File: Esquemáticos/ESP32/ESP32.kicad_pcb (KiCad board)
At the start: 2 copper layers, 100 x 100 mm, 71 parts, among them J1 Conector para bobinas del mot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, J2 Conector para bobinas del mot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, J3 Barrel_Jack, J4 USB Programador, Q1 S8550, Q2 S8550, Q3 S8550, Q4 S8550, Q5 S8550, Q6 S8550, Q7 S8550, Q8 S8550, SW1 SW_DIP_x01, U1 LTV-247, U2 LTV-247, U3 ULN2003A, U4 ULN2003A, U5 AMS1117-5.0, U6 AMS1117-3.3, U7 ESP32-WROOM-32, U8 RFID_RC522

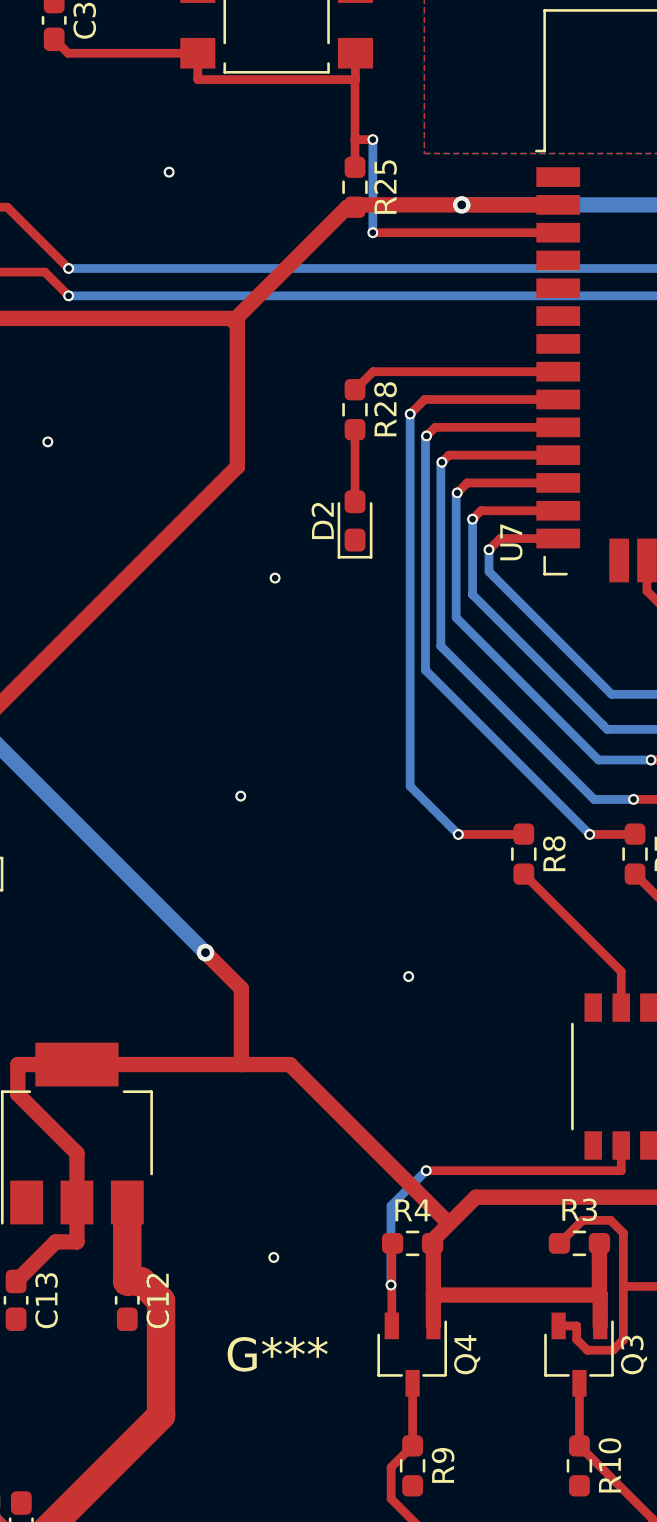
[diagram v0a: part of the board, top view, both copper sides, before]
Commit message: Huellas actualizadas según los vendedores locales
Falta la del optoacoplador y actualizar la placa. Además, dependiendo de la resñpuesta del profe tocaría re-diseñar todo :c
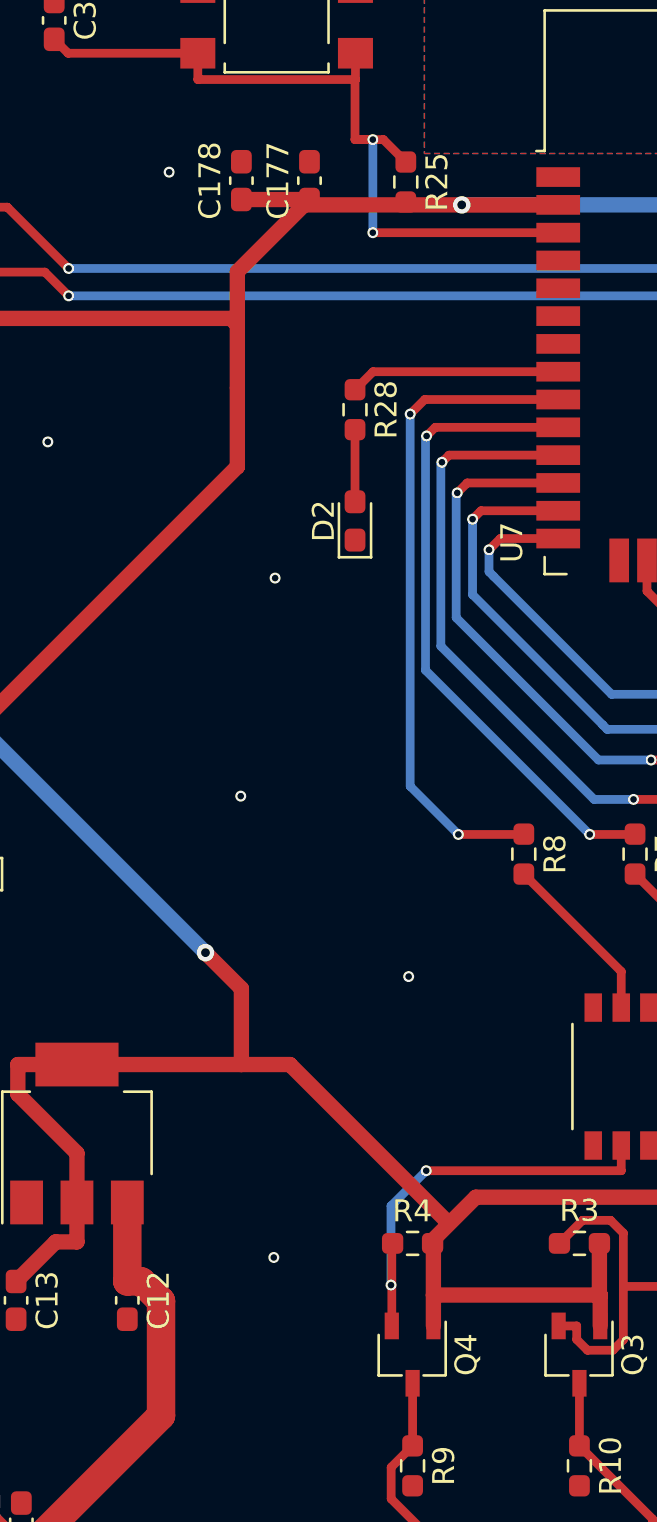
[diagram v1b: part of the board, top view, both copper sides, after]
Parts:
- added C177: 0.1uF, Capacitor_SMD:C_0603_1608Metric_Pad1.08x0.95mm_HandSolder, F.Cu at (130.0, 65.7)
- added C178: 22uF, Capacitor_SMD:C_0603_1608Metric_Pad1.08x0.95mm_HandSolder, F.Cu at (126.9, 65.7)
- moved G*** 30.9 mm to (151.7, 102.6)
- moved R25 2.33 mm to (134.4, 65.8)
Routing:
- net +3.3V: track 184.4 -> 188.7 mm
- net /Principal/EN/RST: track 34.0 -> 35.5 mm

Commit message: NewPCB
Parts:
- removed SW1: SW_DIP_x01, Button_Switch_SMD:SW_DIP_SPSTx01_Slide_6.7x4.1mm_W6.73mm_P2.54mm_LowProfile_JPin
- added JP1: Jumper_3_Open, Connector_PinHeader_2.54mm:PinHeader_1x03_P2.54mm_Vertical, F.Cu at (104.1, 131.2)
- BOOT1, EN1: footprint Button_Switch_SMD:SW_SPST_TL3305A -> Button_Switch_SMD:SW_SPST_B3S-1000
- C1, C2: value 100n -> 0.1uF; footprint Capacitor_SMD:C_0603_1608Metric_Pad1.08x0.95mm_HandSolder -> Capacitor_SMD:C_0805_2012Metric_Pad1.18x1.45mm_HandSolder
- C11, C12, C13, C14, C15, C177, C178: footprint Capacitor_SMD:C_0603_1608Metric_Pad1.08x0.95mm_HandSolder -> Capacitor_SMD:C_0805_2012Metric_Pad1.18x1.45mm_HandSolder
- C3, C4: value 100nF -> 0.1uF; footprint Capacitor_SMD:C_0603_1608Metric_Pad1.08x0.95mm_HandSolder -> Capacitor_SMD:C_0805_2012Metric_Pad1.18x1.45mm_HandSolder
- J3: footprint Connector_BarrelJack:BarrelJack_CLIFF_FC681465S_SMT_Horizontal -> Connector_BarrelJack:BarrelJack_GCT_DCJ200-10-A_Horizontal
- R1, R10, R11, R12, R13, R14, R15, R16, R17, R18, R19, R2, R20, R21, R22, R23, R24, R25, R26, R27, R3, R4, R5, R6, R7, R8, R9: footprint Resistor_SMD:R_0603_1608Metric_Pad0.98x0.95mm_HandSolder -> Resistor_SMD:R_0805_2012Metric_Pad1.20x1.40mm_HandSolder
- R28, R29: value 56 -> 68; footprint Resistor_SMD:R_0603_1608Metric_Pad0.98x0.95mm_HandSolder -> Resistor_SMD:R_1206_3216Metric_Pad1.30x1.75mm_HandSolder
- U1, U2: footprint Package_SO:SOP-16_4.4x10.4mm_P1.27mm -> Package_DIP:DIP-16_W7.62mm_Socket
- U3, U4: footprint Package_SO:SOIC-16_4.55x10.3mm_P1.27mm -> Package_DIP:DIP-16_W7.62mm_Socket
- moved U4 15.2 mm to (191.7, 130.7)
- moved H3 12.2 mm to (117.9, 140.4)
- moved U2 11.1 mm to (187.7, 101.4)
- moved U3 11.1 mm to (156.6, 130.9)
- moved U1 10.8 mm to (157.0, 101.6)
- moved J3 5.88 mm to (105.5, 137.7), turned to 0 degrees
- moved C1 5.02 mm to (133.5, 133.8)
- moved C2 3.45 mm to (167.4, 133.7)
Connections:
- J3 pad 3: (no net) -> GND
- J4 pad 3: Net-(J4-Pad3) -> /Principal/TX
- J4 pad 4: Net-(J4-Pad4) -> /Principal/RX
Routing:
- net Net-(Q4-Pad2): track 19.8 -> 0.00 mm, vias 2 -> 0
- net +5V: track 178.9 -> 198.7 mm, vias 1 -> 3
- net unconnected-(JP1-Pad1): track 0.00 -> 14.3 mm
- net Net-(J3-Pad1): track 14.3 -> 0.00 mm

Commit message: PCB terminada
Revisar los gerber y los drill :3
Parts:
- removed RRX1, RTX1: R, Resistor_SMD:R_0603_1608Metric_Pad0.98x0.95mm_HandSolder
- moved G*** 29.9 mm to (121.8, 103.2)
- moved C11 6.99 mm to (112.0, 132.0), turned to -90 degrees
- moved H3 5.60 mm to (118.1, 146.0)
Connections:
- C1 pad 1: +12V -> +5V
- C2 pad 1: +12V -> +5V
- J1 pad 1: +12V -> +5V
- J2 pad 1: +12V -> +5V
- U3 pad 9: +12V -> +5V
- U4 pad 9: +12V -> +5V
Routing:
- net +12V: track 153.3 -> 36.8 mm
- net +5V: track 198.7 -> 303.2 mm, vias 3 -> 0
- net +3.3V: track 188.7 -> 163.4 mm, vias 2 -> 3
- net /Principal/SCK: track 39.2 -> 60.5 mm, vias 1 -> 0
- net /Principal/MISO: track 35.3 -> 54.1 mm
- net /Motores/Out1: track 25.9 -> 10.9 mm, vias 3 -> 0
- net /Motores/In8: track 44.9 -> 59.4 mm, vias 2 -> 0
- net unconnected-(JP1-Pad1): track 14.3 -> 0.00 mm
- net Net-(Q4-Pad2): track 0.00 -> 14.2 mm
- net Net-(Q7-Pad2): track 24.0 -> 11.1 mm, vias 2 -> 0
- net Net-(J3-Pad1): track 0.00 -> 12.5 mm
- net Net-(Q5-Pad2): track 20.9 -> 9.16 mm
- net Net-(Q3-Pad2): track 22.2 -> 11.7 mm, vias 2 -> 0
- net Net-(J2-Pad2): track 7.68 -> 16.1 mm
- net Net-(J2-Pad3): track 8.19 -> 16.0 mm
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
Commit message: PCB lista uwu
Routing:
- net Net-(Q2-Pad2): track 12.7 -> 10.1 mm
- net +3.3V: track 163.4 -> 161.3 mm
- net Net-(J2-Pad4): track 16.0 -> 14.9 mm
- net Net-(J1-Pad2): track 12.4 -> 11.5 mm
- net Net-(J3-Pad1): track 12.5 -> 11.8 mm
- net /Principal/TX: track 60.6 -> 61.1 mm

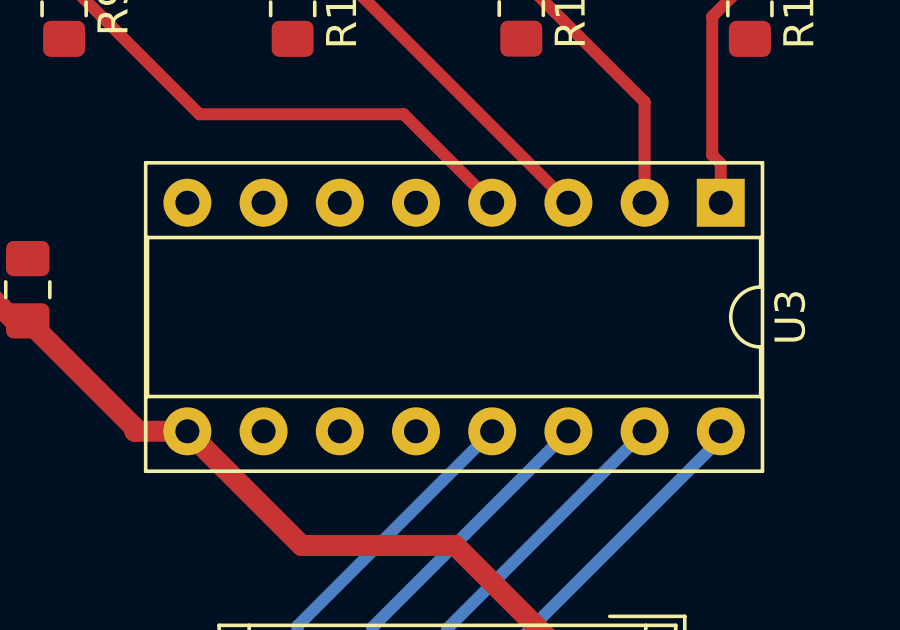
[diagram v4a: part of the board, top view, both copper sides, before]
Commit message: Numero de Orden añadido
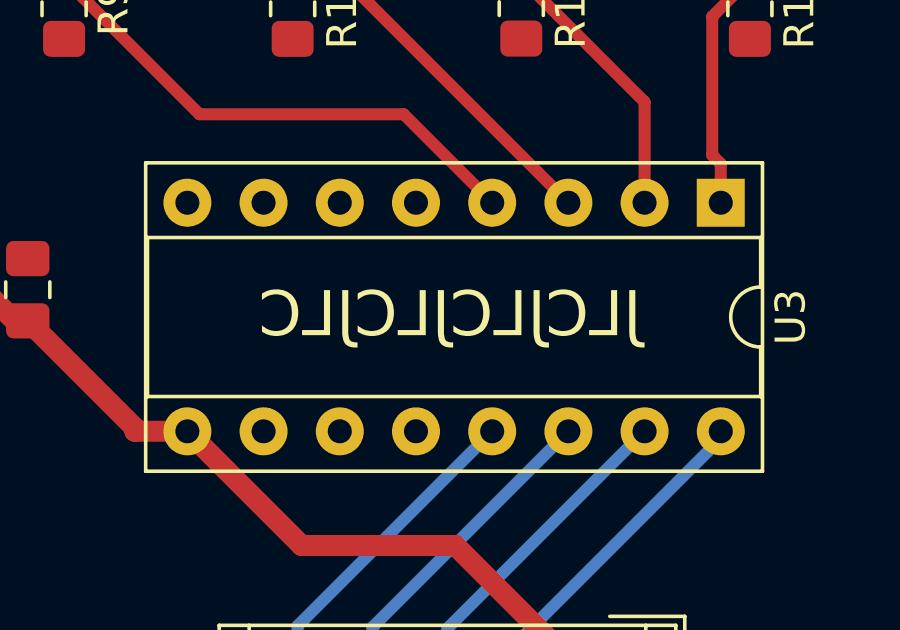
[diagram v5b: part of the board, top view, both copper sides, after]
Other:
- board text added: "JLCJLCJLCJLC"
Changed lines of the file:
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@@
     (effects (font (size 1 1) (thickness 0.15)))
+  )
+  (gr_text "JLCJLCJLCJLC" (at 147.574 134.62) (layer "F.SilkS")
+    (effects (font (size 1.5 1.5) (thickness 0.3)) (justify mirror))
   )
   (gr_text "IRQ" (at 197.25 76) (layer "F.SilkS")
